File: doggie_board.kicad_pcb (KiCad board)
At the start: 4 copper layers, 117.6 x 127 mm, 110 parts, among them J1 Conn_01x03, J2 XT90PW-M, J3 XT90PW-M, J4 Conn_01x02, J5 Conn_01x03, J5V1 48v, J5V10 48v, J5V11 48v, J5V12 48v, J5V13 12v, J5V14 12v, J5V15 12v, J5V16 12v, J5V17 3.3v, J5V18 3.3v, J5V19 3.3v, J5V2 48v, J5V20 3.3v, J5V21 5v, J5V22 5v, J5V23 5v, J5V24 5v, J5V3 48v, J5V4 48v, J5V5 48v, J5V6 48v, J5V7 48v, J5V8 48v, J5V9 48v, J6 Conn_01x02, J7 Conn_01x03, J8 Conn_01x03, Q1 PSMN3R7-100BSEJ, Q10 2N7002, Q11 2N7002, Q12 2N7002, Q2 PSMN3R7-100BSEJ, Q3 PSMN3R7-100BSEJ, Q4 PSMN3R7-100BSEJ, Q5 PSMN3R7-100BSEJ, Q6 PSMN3R7-100BSEJ, Q7 Q_NMOS, Q8 Q_NMOS, Q9 2N7002, SW1 SW_SPST, U1 TPS2490, U2 LM5148RGYR, U3 TPS566242DRLR, U4 TPS566242DRLR

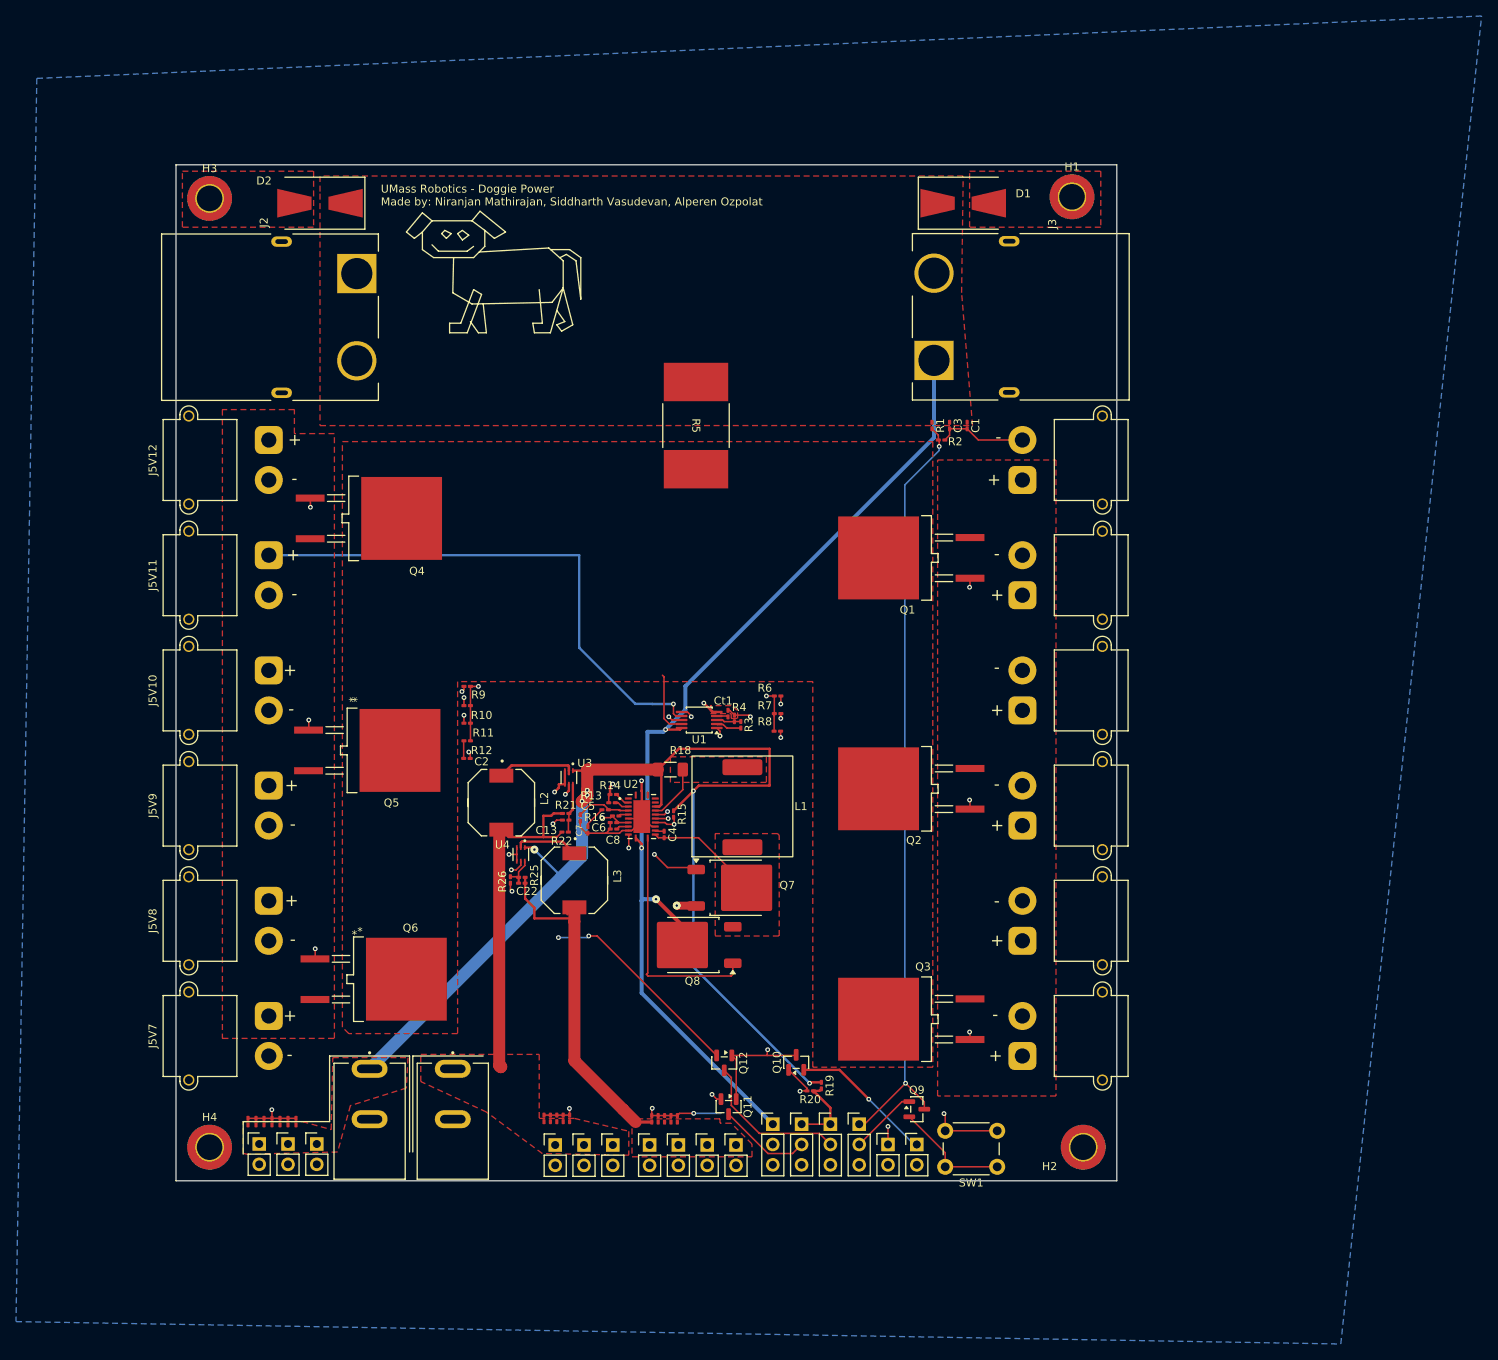
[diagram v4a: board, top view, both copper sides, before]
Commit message: added switch and cleaned up board a little
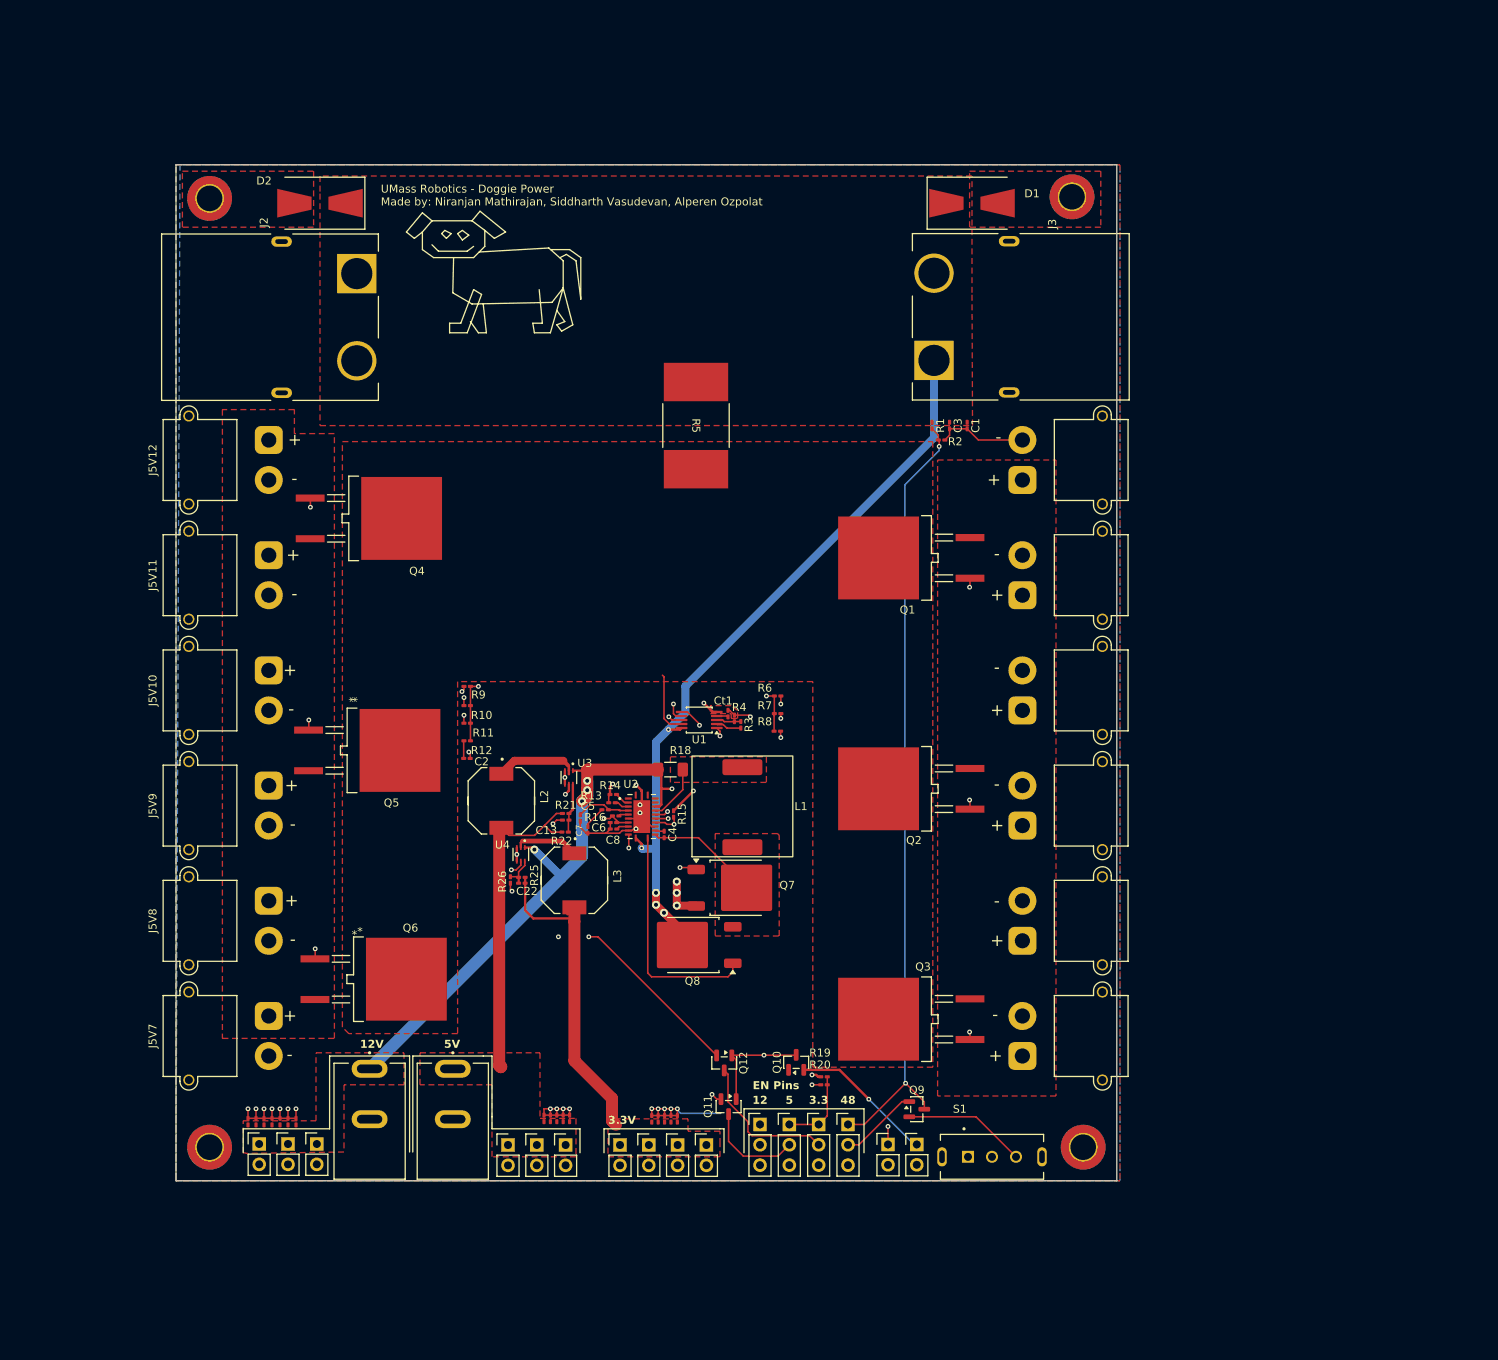
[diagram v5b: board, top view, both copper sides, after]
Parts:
- removed SW1: SW_SPST, Button_Switch_THT:SW_PUSH_6mm
- added S1: SLW-129956-4A-RA-N-D, footprints:SW_SLW-129956-4A-RA-N-D, F.Cu at (141.6, 162.6)
- moved J5V22 5.90 mm to (88.3, 161.1)
- moved J5V23 5.90 mm to (81.1, 161.1)
- moved J5V24 5.90 mm to (84.7, 161.1)
- moved J5V17 3.70 mm to (98.7, 161.1)
- moved J5V18 3.70 mm to (102.3, 161.1)
- moved J5V20 3.70 mm to (95.1, 161.1)
- moved J5V19 3.70 mm to (105.9, 161.1)
- moved R20 1.89 mm to (120.6, 153.6)
- moved J5 1.60 mm to (112.6, 158.6)
- moved J7 1.53 mm to (116.3, 158.6)
- moved J8 1.47 mm to (119.9, 158.6)
- moved J1 1.40 mm to (123.6, 158.6)
- moved R19 1.15 mm to (120.6, 152.6), turned to 0 degrees
- moved D1 1.10 mm to (139.1, 43.4)
- moved L2 0.23 mm to (80.3, 118.1)
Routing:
- net +12V: track 150.4 -> 125.0 mm, vias 6 -> 7
- net GND: track 76.6 -> 93.2 mm, vias 15 -> 32
- net +3.3V: track 44.1 -> 41.5 mm
- net +48V: track 123.1 -> 120.5 mm
- net 48_RAW: track 132.7 -> 130.9 mm, vias 3 -> 5
- net +5V: track 43.3 -> 41.8 mm
- net /High Side Power Switch/sw_low: track 96.3 -> 97.7 mm
- net Net-(J1-Pin_2): track 8.48 -> 9.90 mm
- net 12V_PG: track 52.0 -> 50.9 mm
- net ps_sw: track 68.7 -> 67.8 mm, vias 2 -> 1
- net Net-(Q9-S): track 14.6 -> 15.4 mm
- net /3.3v Buck Converter/3V3_EN: track 19.1 -> 18.4 mm
- net /5v Buck Converter/5V_EN: track 11.6 -> 12.3 mm
- net /12v Buck Converter/12V_EN: track 50.0 -> 49.4 mm
- added copper zone on In1.Cu, net GND
- added copper zone on In2.Cu, net GND
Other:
- board text added: "12"
- board text added: "12V"
- board text added: "3.3"
- board text added: "3.3V"
- board text added: "48"
- board text added: "5"
- board text added: "5V"
- board text added: "EN Pins"

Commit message: fixed footprintns
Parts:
- C1, C10, C11, C12, C13, C14, C15, C16, C17, C18, C19, C2, C20, C21, C22, C23, C24, C25, C26, C27, C3, C4, C5, C6, C7, C8, C9, Ct1: footprint Capacitor_SMD:C_0201_0603Metric_Pad0.64x0.40mm_HandSolder -> Capacitor_SMD:C_0603_1608Metric_Pad1.08x0.95mm_HandSolder
- R1, R10, R11, R12, R13, R14, R15, R16, R17, R19, R2, R20, R21, R22, R25, R26, R3, R4, R6, R7, R8, R9: footprint Resistor_SMD:R_0201_0603Metric_Pad0.64x0.40mm_HandSolder -> Resistor_SMD:R_0603_1608Metric_Pad0.98x0.95mm_HandSolder
- moved R15 23.6 mm to (103.3, 143.3), turned to 0 degrees
- moved C12 9.67 mm to (57.9, 149.6)
- moved C18 6.66 mm to (81.0, 153.9), turned to 0 degrees
- moved C9 6.03 mm to (57.1, 152.7), turned to 180 degrees
- moved C17 5.40 mm to (81.8, 157.6)
- moved R16 5.09 mm to (91.5, 124.1), turned to 90 degrees
- moved C16 4.60 mm to (83.4, 157.6)
- moved L3 4.35 mm to (92.0, 131.5)
- moved C15 3.81 mm to (85.0, 157.6)
- moved C11 3.69 mm to (56.2, 157.4)
- moved C2 3.66 mm to (79.1, 110.9), turned to 90 degrees
- moved C6 3.49 mm to (93.1, 124.1), turned to -90 degrees
- moved C10 3.10 mm to (54.6, 157.4)
- moved U3 2.91 mm to (85.8, 115.2)
- moved R22 2.85 mm to (86.4, 118.4)
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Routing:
- net /12v Buck Converter/VDDA: track 13.5 -> 23.7 mm
- net Net-(Q1-Pad1): track 36.1 -> 28.6 mm
- net +12V: track 125.0 -> 132.2 mm
- net Net-(U2-FB): track 1.24 -> 5.98 mm
- net +5V: track 41.8 -> 37.2 mm
- net 48_RAW: track 130.9 -> 135.3 mm
- net /12v Buck Converter/switch 12v: track 14.1 -> 17.9 mm
- net /5v Buck Converter/SW: track 10.4 -> 6.56 mm
- net Net-(U1-PROG): track 3.09 -> 6.14 mm
- net /3.3v Buck Converter/SW: track 8.43 -> 11.4 mm
- net +3.3V: track 41.5 -> 38.6 mm
- net Net-(Q2-Pad1): track 29.6 -> 27.1 mm
- net Net-(U2-EXTCOMP): track 6.95 -> 4.66 mm
- net Net-(Q6-Pad1): track 39.2 -> 37.0 mm
- net /High Side Power Switch/gate_line: track 66.1 -> 68.0 mm
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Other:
- board text added: "12V @ 7A"
- board text added: "5V @ 6A"
- board text removed: "12V"
- board text removed: "5V"

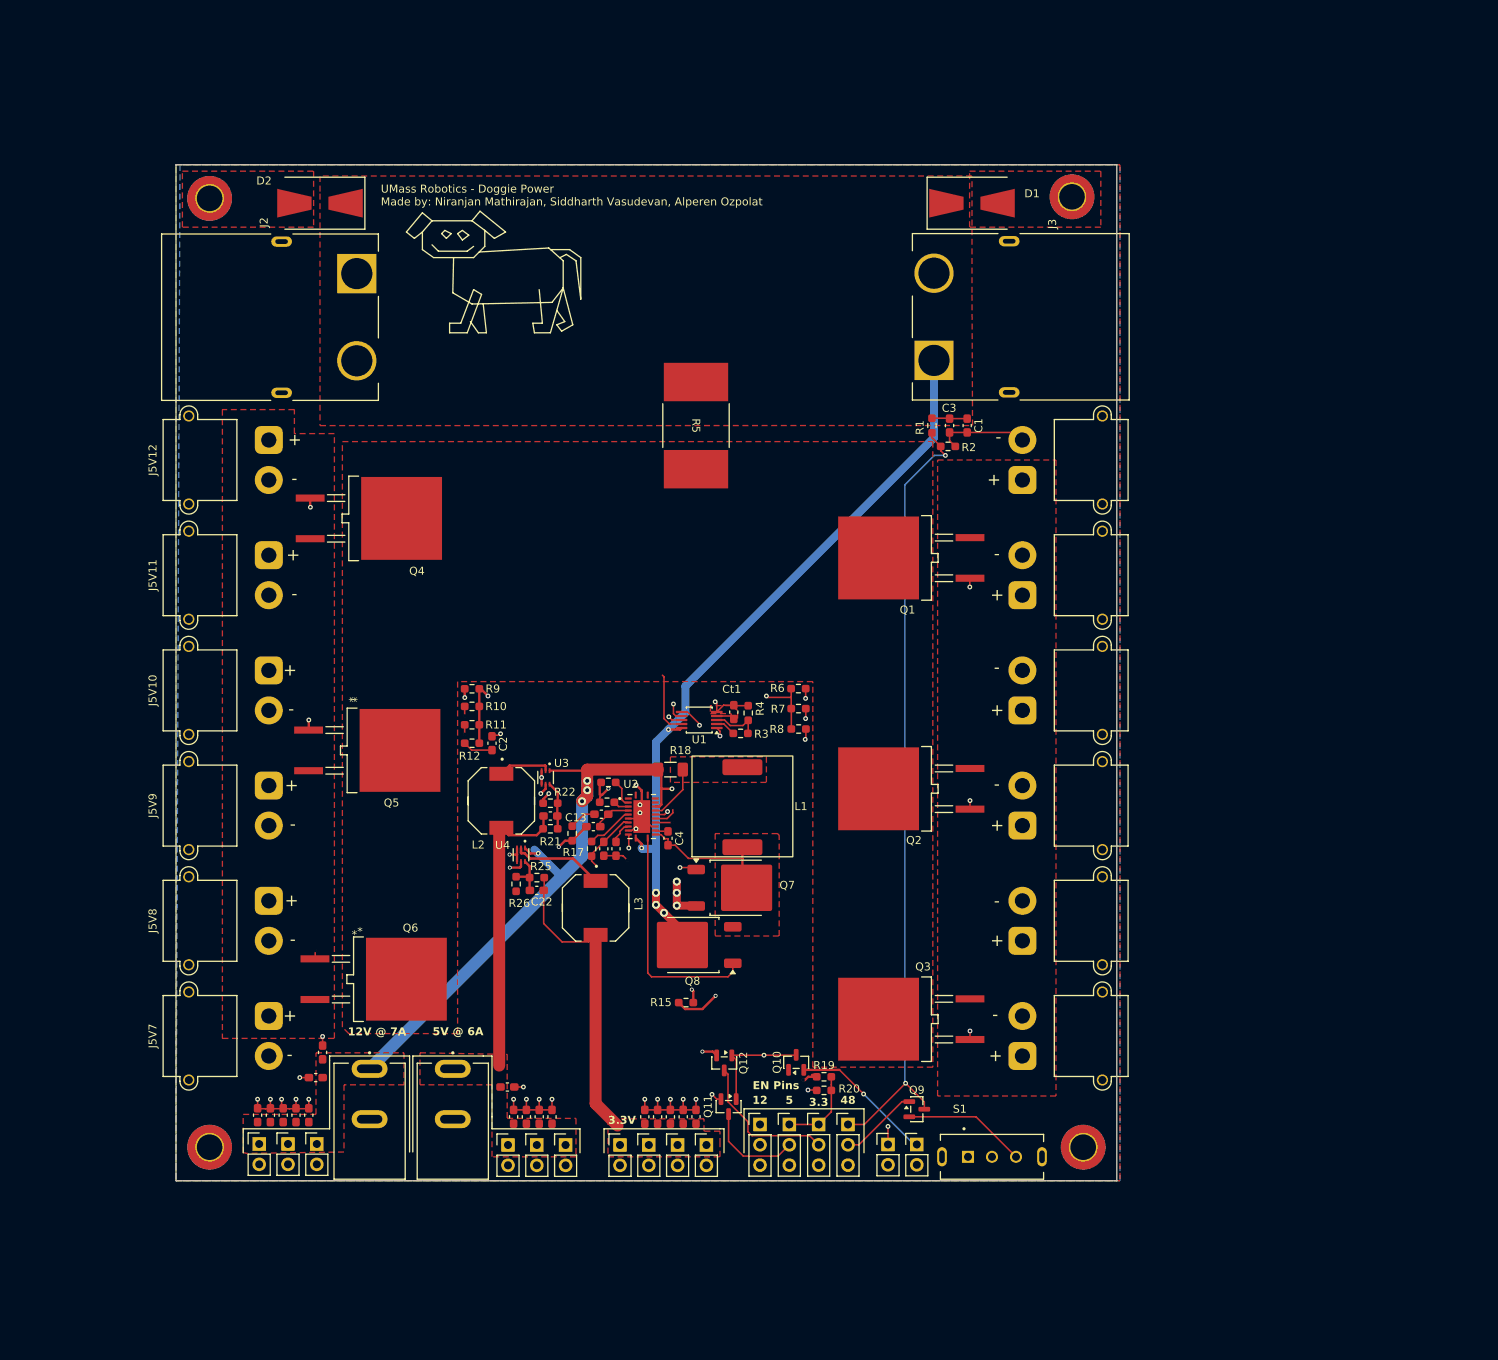
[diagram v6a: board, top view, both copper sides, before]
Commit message: fixed vias and added stitching
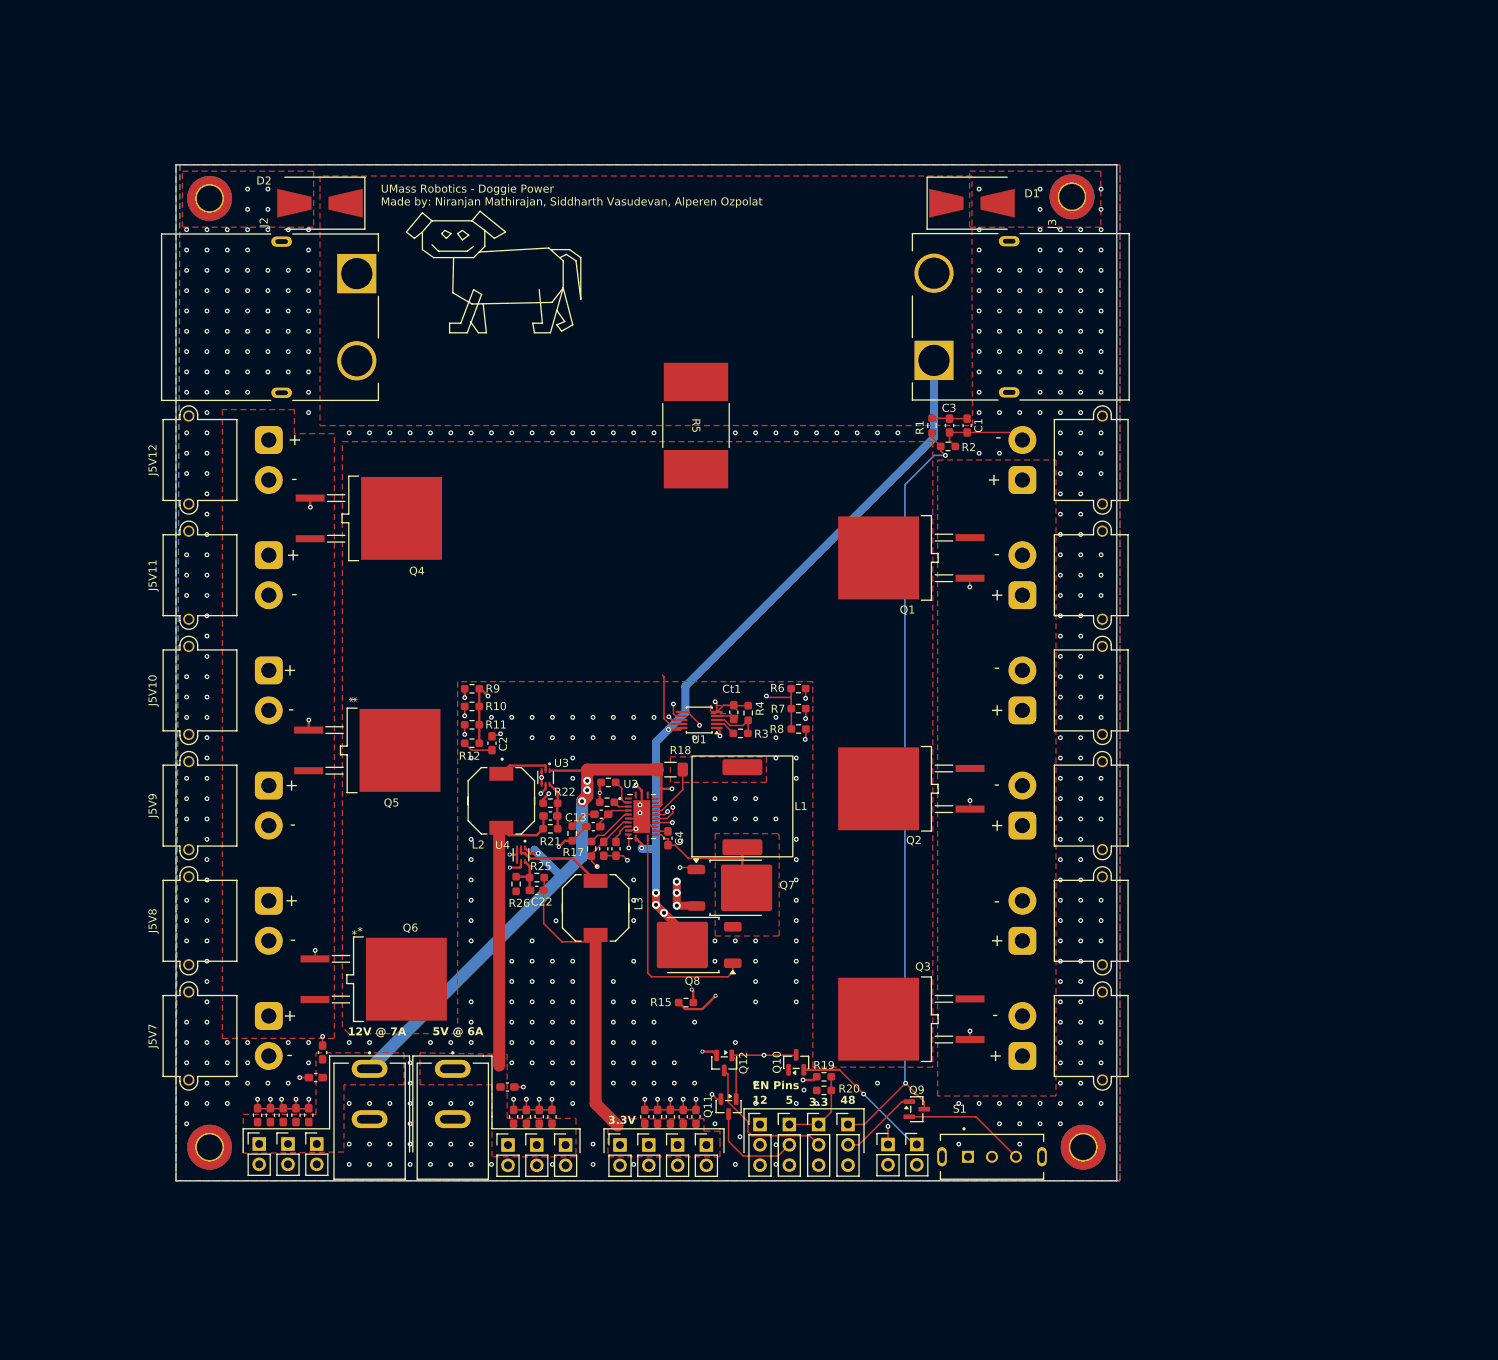
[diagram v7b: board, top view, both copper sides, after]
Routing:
- net GND: track 91.5 -> 89.0 mm, vias 33 -> 510
- net +12V: track 132.2 -> 131.7 mm
